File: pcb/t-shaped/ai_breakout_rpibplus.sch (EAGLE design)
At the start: 5 parts, among them J1 1X20, J2 1X20NOFIRST, J3 2X20-RPI-BRK

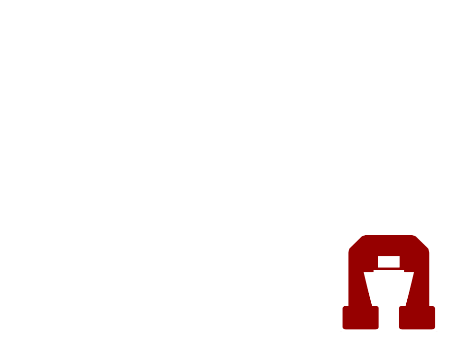
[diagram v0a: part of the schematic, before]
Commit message: Updating T-Shaped.  Added a few labels to R-Shaped
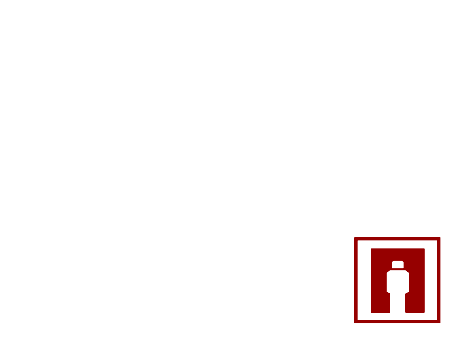
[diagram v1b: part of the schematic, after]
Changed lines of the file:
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@@
 <part name="FRAME1" library="Ai_Miscellany" deviceset="FRAME-LETTER" device="">
 <attribute name="AUTHOR" value="A.I. HARDWARE SITH LORDS"/>
-<attribute name="REV" value="1.0"/>
+<attribute name="REV" value="1.1"/>
 </part>
 <part name="J3" library="Ai_Connectors" deviceset="2X20-RPI" device="-BRK"/>
@@
 <instance part="GND1" gate="GND" x="107.95" y="77.47"/>
 <instance part="GND2" gate="GND" x="134.62" y="77.47"/>
-<instance part="U$1" gate="G$1" x="138.43" y="17.78"/>
-<instance part="U$2" gate="G$1" x="138.43" y="17.78" rot="MR0"/>
+<instance part="U$1" gate="G$1" x="134.62" y="13.97"/>
+<instance part="U$2" gate="G$1" x="134.62" y="13.97"/>
 </instances>
 <busses>
